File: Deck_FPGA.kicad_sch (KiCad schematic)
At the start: 70 parts, among them J1 Left side, J2 Right Side, J3 Conn_01x06, U1 XC7A100T-CSG324, U2 TPS65023BRSBT, U3 S25FL128SAGNFI000, U4 LM3880, X1 ASE-100MHz

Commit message: added PowerIC filtering resistor and pull up for SPI Flash SIO2/SIO3
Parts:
- added R24, R25: 4k7, Resistor_SMD:R_0402_1005Metric, symbol Device:R
- added R26: 10R, Resistor_SMD:R_0402_1005Metric, symbol Device:R
- C22, C25, C32: value 10u -> 22u
- R14, R15: value 100k -> 4k7
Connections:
- net +3V3: now also R24.2, R25.1
- net SIO2: now also R24.1
- net SIO3: now also R25.2
- net VBUS: now also R26.1; no longer C24.1, U2.37 (VCC)
- new net VCC: C24.1, R26.2, U2.37 (VCC)

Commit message: jlc references
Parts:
- C29: value 100nF -> 100n
- C30: value 100n -> 470n
- D1: value LED -> LED_RED; LCSC (none) -> C5879214
- D2: value LED -> LED_BLUE; LCSC (none) -> C5879217
- D3: value LED -> LED_YELLOW; LCSC (none) -> C5879216
- L1: LCSC (none) -> C2047319
- R11: value 100K -> 100k
- R12: value 150K -> 150k
- R13: value 10k -> 4k7
- R22, R23, R7: value 200 -> 200R
- R8: value 100 -> 100R
- U1: LCSC (none) -> C5181214
- U2: LCSC (none) -> C138723
- U3: LCSC (none) -> C22445046
- U4: LCSC (none) -> C2650186
- X1: LCSC (none) -> C596959
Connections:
- net +1V8: now also L2.2; no longer L2.1
- net L2: now also L2.1; no longer L2.2
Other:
- moved on the sheet: L2

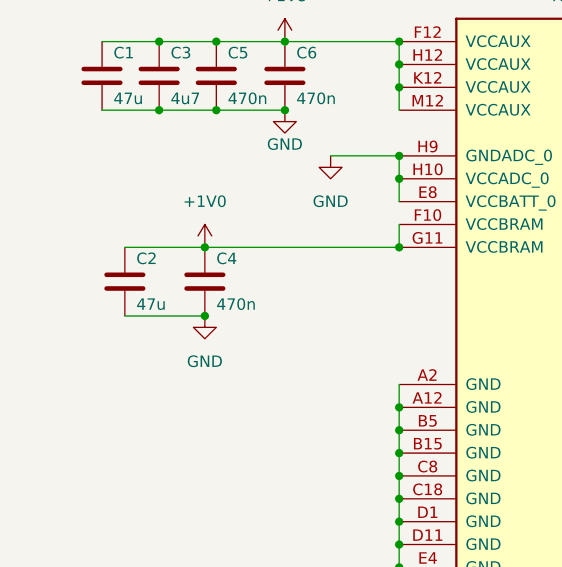
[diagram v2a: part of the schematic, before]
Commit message: fixed caps, jlc references
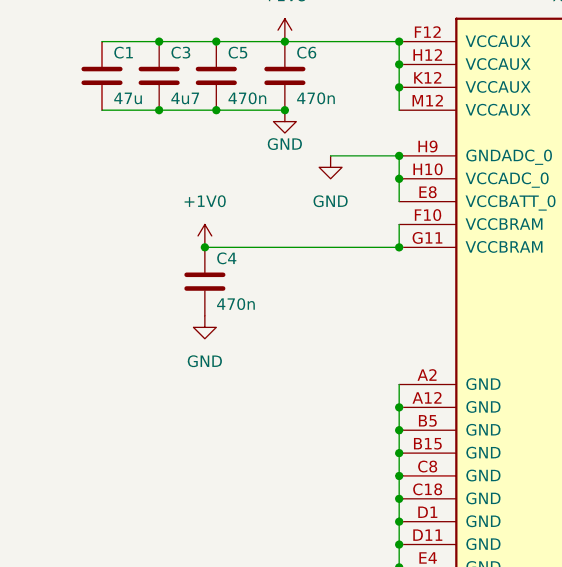
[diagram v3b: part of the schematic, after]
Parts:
- removed C2: 47u, Capacitor_SMD:C_0402_1005Metric, symbol Device:C
- C1: footprint Capacitor_SMD:C_0402_1005Metric -> Capacitor_SMD:C_0603_1608Metric; LCSC (none) -> C140782
- C15, C19, C7: footprint Capacitor_SMD:C_0402_1005Metric -> Capacitor_SMD:C_0603_1608Metric
- C16, C3: LCSC (none) -> C23733
- C22, C25: LCSC (none) -> C86295
- C24: LCSC (none) -> C15849
- C29: LCSC (none) -> C60474
- C4: LCSC (none) -> C106255
- R1: LCSC (none) -> C11702
- R12: LCSC (none) -> C2909320
- R26: LCSC (none) -> C413044
- R4: LCSC (none) -> C25900
- R7: LCSC (none) -> C25087
- R8: LCSC (none) -> C25076
- R9: LCSC (none) -> C2906859
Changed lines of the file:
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@@
   (junction (at 501.65 119.38) (diameter 0) (color 0 0 0 0)
   )
-  (junction (at 41.91 308.61) (diameter 0) (color 0 0 0 0)
-  )
   (junction (at 220.98 107.95) (diameter 0) (color 0 0 0 0)
   )
@@
     (stroke (width 0) (type default) (color 0 0 0 0))
   )
-  (wire (pts (xy 33.02 308.61) (xy 41.91 308.61))
-    (stroke (width 0) (type default) (color 0 0 0 0))
-  )
   (wire (pts (xy 410.21 334.01) (xy 415.29 334.01))
     (stroke (width 0) (type default) (color 0 0 0 0))
@@
     (stroke (width 0) (type default) (color 0 0 0 0))
   )
-  (wire (pts (xy 33.02 300.99) (xy 41.91 300.99))
-    (stroke (width 0) (type default) (color 0 0 0 0))
-  )
   (wire (pts (xy 314.96 285.75) (xy 314.96 298.45))
     (stroke (width 0) (type default) (color 0 0 0 0))
@@
       (effects (font (size 1.27 1.27)) (justify left))
     )
-    (property "Footprint" "Capacitor_SMD:C_0402_1005Metric" (id 2) (at 65.7352 25.4 0)
+    (property "Footprint" "Capacitor_SMD:C_0603_1608Metric" (id 2) (at 65.7352 25.4 0)
       (effects (font (size 1.27 1.27)) hide)
     )
@@
       (effects (font (size 1.27 1.27)) (justify left))
     )
-    (property "Footprint" "Capacitor_SMD:C_0402_1005Metric" (id 2) (at 126.6952 285.75 0)
+    (property "Footprint" "Capacitor_SMD:C_0603_1608Metric" (id 2) (at 126.6952 285.75 0)
       (effects (font (size 1.27 1.27)) hide)
     )
@@
       (effects (font (size 1.27 1.27)) (justify left))
     )
-    (property "Footprint" "Capacitor_SMD:C_0402_1005Metric" (id 2) (at 31.4452 285.75 0)
+    (property "Footprint" "Capacitor_SMD:C_0603_1608Metric" (id 2) (at 31.4452 285.75 0)
       (effects (font (size 1.27 1.27)) hide)
     )
@@
       (effects (font (size 1.27 1.27)) hide)
     )
+    (property "LCSC" "C140782" (id 4) (at 30.48 281.94 0)
+      (effects (font (size 1.27 1.27)) hide)
+    )
     (pin "1")
     (pin "2")
@@
       (effects (font (size 1.27 1.27)) hide)
     )
+    (property "LCSC" "C106255" (id 4) (at 41.91 304.8 0)
+      (effects (font (size 1.27 1.27)) hide)
+    )
     (pin "1")
     (pin "2")
@@
       (effects (font (size 1.27 1.27)) hide)
     )
+    (property "LCSC" "C413044" (id 4) (at 326.39 285.75 90)
+      (effects (font (size 1.27 1.27)) hide)
+    )
     (pin "1")
     (pin "2")
@@
       (effects (font (size 1.27 1.27)) hide)
     )
+    (property "LCSC" "C15849" (id 4) (at 337.82 289.56 0)
+      (effects (font (size 1.27 1.27)) hide)
+    )
     (pin "1")
     (pin "2")
@@
       (effects (font (size 1.27 1.27)) hide)
     )
+    (property "LCSC" "C11702" (id 4) (at 240.03 337.82 90)
+      (effects (font (size 1.27 1.27)) hide)
+    )
     (pin "1")
     (pin "2")
@@
       (effects (font (size 1.27 1.27)) hide)
     )
+    (property "LCSC" "C25087" (id 4) (at 278.13 344.17 0)
+      (effects (font (size 1.27 1.27)) hide)
+    )
     (pin "1")
     (pin "2")
@@
     (pin "1")
   )
-  (symbol (lib_id "Device:C") (at 33.02 304.8 0) (unit 1)
-    (in_bom yes) (on_board yes)
-    (property "Reference" "C2" (id 0) (at 34.29 302.26 0)
-      (effects (font (size 1.27 1.27)) (justify left))
-    )
-    (property "Value" "47u" (id 1) (at 34.29 307.34 0)
-      (effects (font (size 1.27 1.27)) (justify left))
-    )
-    (property "Footprint" "Capacitor_SMD:C_0402_1005Metric" (id 2) (at 33.9852 308.61 0)
-      (effects (font (size 1.27 1.27)) hide)
-    )
-    (property "Datasheet" "~" (id 3) (at 33.02 304.8 0)
-      (effects (font (size 1.27 1.27)) hide)
-    )
-    (pin "1")
-    (pin "2")
-  )
   (symbol (lib_id "power:PWR_FLAG") (at 345.44 245.11 90) (unit 1)
     (in_bom yes) (on_board yes) (fields_autoplaced)
@@
       (effects (font (size 1.27 1.27)) hide)
     )
+    (property "LCSC" "C23733" (id 4) (at 133.35 281.94 0)
+      (effects (font (size 1.27 1.27)) hide)
+    )
     (pin "1")
     (pin "2")
@@
       (effects (font (size 1.27 1.27)) hide)
     )
+    (property "LCSC" "C2906859" (id 4) (at 332.74 318.77 90)
+      (effects (font (size 1.27 1.27)) hide)
+    )
     (pin "1")
     (pin "2")
@@
       (effects (font (size 1.27 1.27)) hide)
     )
+    (property "LCSC" "C60474" (id 4) (at 483.87 356.87 0)
+      (effects (font (size 1.27 1.27)) hide)
+    )
     (pin "1")
     (pin "2")
@@
       (effects (font (size 1.27 1.27)) (justify left))
     )
-    (property "Footprint" "Capacitor_SMD:C_0402_1005Metric" (id 2) (at 223.2152 304.8 0)
+    (property "Footprint" "Capacitor_SMD:C_0603_1608Metric" (id 2) (at 223.2152 304.8 0)
       (effects (font (size 1.27 1.27)) hide)
     )
@@
       (effects (font (size 1.27 1.27)) hide)
     )
+    (property "LCSC" "C25076" (id 4) (at 278.13 351.79 0)
+      (effects (font (size 1.27 1.27)) hide)
+    )
     (pin "1")
     (pin "2")
@@
       (effects (font (size 1.27 1.27)) hide)
     )
+    (property "LCSC" "C86295" (id 4) (at 322.58 302.26 0)
+      (effects (font (size 1.27 1.27)) hide)
+    )
     (pin "1")
     (pin "2")
@@
       (effects (font (size 1.27 1.27)) hide)
     )
+    (property "LCSC" "C25900" (id 4) (at 246.38 350.52 90)
+      (effects (font (size 1.27 1.27)) hide)
+    )
     (pin "1")
     (pin "2")
@@
       (effects (font (size 1.27 1.27)) hide)
     )
+    (property "LCSC" "C86295" (id 4) (at 337.82 302.26 0)
+      (effects (font (size 1.27 1.27)) hide)
+    )
     (pin "1")
     (pin "2")
@@
       (effects (font (size 1.27 1.27)) hide)
     )
+    (property "LCSC" "C23733" (id 4) (at 36.83 281.94 0)
+      (effects (font (size 1.27 1.27)) hide)
+    )
     (pin "1")
     (pin "2")
@@
       (effects (font (size 1.27 1.27)) hide)
     )
+    (property "LCSC" "C2909320" (id 4) (at 340.36 375.92 0)
+      (effects (font (size 1.27 1.27)) hide)
+    )
     (pin "1")
     (pin "2")
@@
     )
     (path "/22a99473-3e55-4b82-8223-740f01d7295e"
-      (reference "C1") (unit 1) (value "47u") (footprint "Capacitor_SMD:C_0402_1005Metric")
-    )
-    (path "/531d2d7d-53fd-4bcb-834d-f2c3da465c38"
-      (reference "C2") (unit 1) (value "47u") (footprint "Capacitor_SMD:C_0402_1005Metric")
+      (reference "C1") (unit 1) (value "47u") (footprint "Capacitor_SMD:C_0603_1608Metric")
     )
     (path "/f40f7587-767c-4043-9317-011c3c323e01"
@@
     )
     (path "/0597bd17-91c5-49ea-a011-3c120355c323"
-      (reference "C7") (unit 1) (value "47u") (footprint "Capacitor_SMD:C_0402_1005Metric")
+      (reference "C7") (unit 1) (value "47u") (footprint "Capacitor_SMD:C_0603_1608Metric")
     )
     (path "/c0b5a831-b0f8-4592-9d50-a2bbf1143104"
@@
     )
     (path "/18789848-890e-43aa-86a9-1e0060f7c12c"
-      (reference "C15") (unit 1) (value "47u") (footprint "Capacitor_SMD:C_0402_1005Metric")
+      (reference "C15") (unit 1) (value "47u") (footprint "Capacitor_SMD:C_0603_1608Metric")
     )
     (path "/6f2ed173-ac42-4b90-a228-00e14d8db9d7"
@@
     )
     (path "/b3c5cee8-8e81-446f-8212-b1bdfd796e73"
-      (reference "C19") (unit 1) (value "47u") (footprint "Capacitor_SMD:C_0402_1005Metric")
+      (reference "C19") (unit 1) (value "47u") (footprint "Capacitor_SMD:C_0603_1608Metric")
     )
     (path "/254a2134-f3ac-4d6e-a57b-ebf6f160e393"

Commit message: more modifications for jlc
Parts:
- L1: LCSC C2047319 -> C71386
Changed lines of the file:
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@@
       (effects (font (size 1.27 1.27)) hide)
     )
-    (property "LCSC" "C2047319" (id 4) (at 416.56 300.99 90)
+    (property "LCSC" "C71386" (id 4) (at 416.56 300.99 90)
       (effects (font (size 1.27 1.27)) hide)
     )
